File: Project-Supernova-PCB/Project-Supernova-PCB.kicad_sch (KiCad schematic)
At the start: 32 parts, among them J1 Conn_01x04, J103 Screw_Terminal_01x02, J104 Conn_01x02, J105 Conn_01x02, J106 Screw_Terminal_01x02, J107 Conn_Coaxial, J108 Conn_01x04, J109 Screw_Terminal_01x02, J6 100k_Thermistor, J7 100k_Thermistor, Q101 Si1470DH, SW1 SW_SPDT, U1 S09, U101 BMP280-Module, U102 GY-NEO6MV2-Module, U103 LoRa-E5, U2 ESP32-Module-30Pin, U3 LM335D

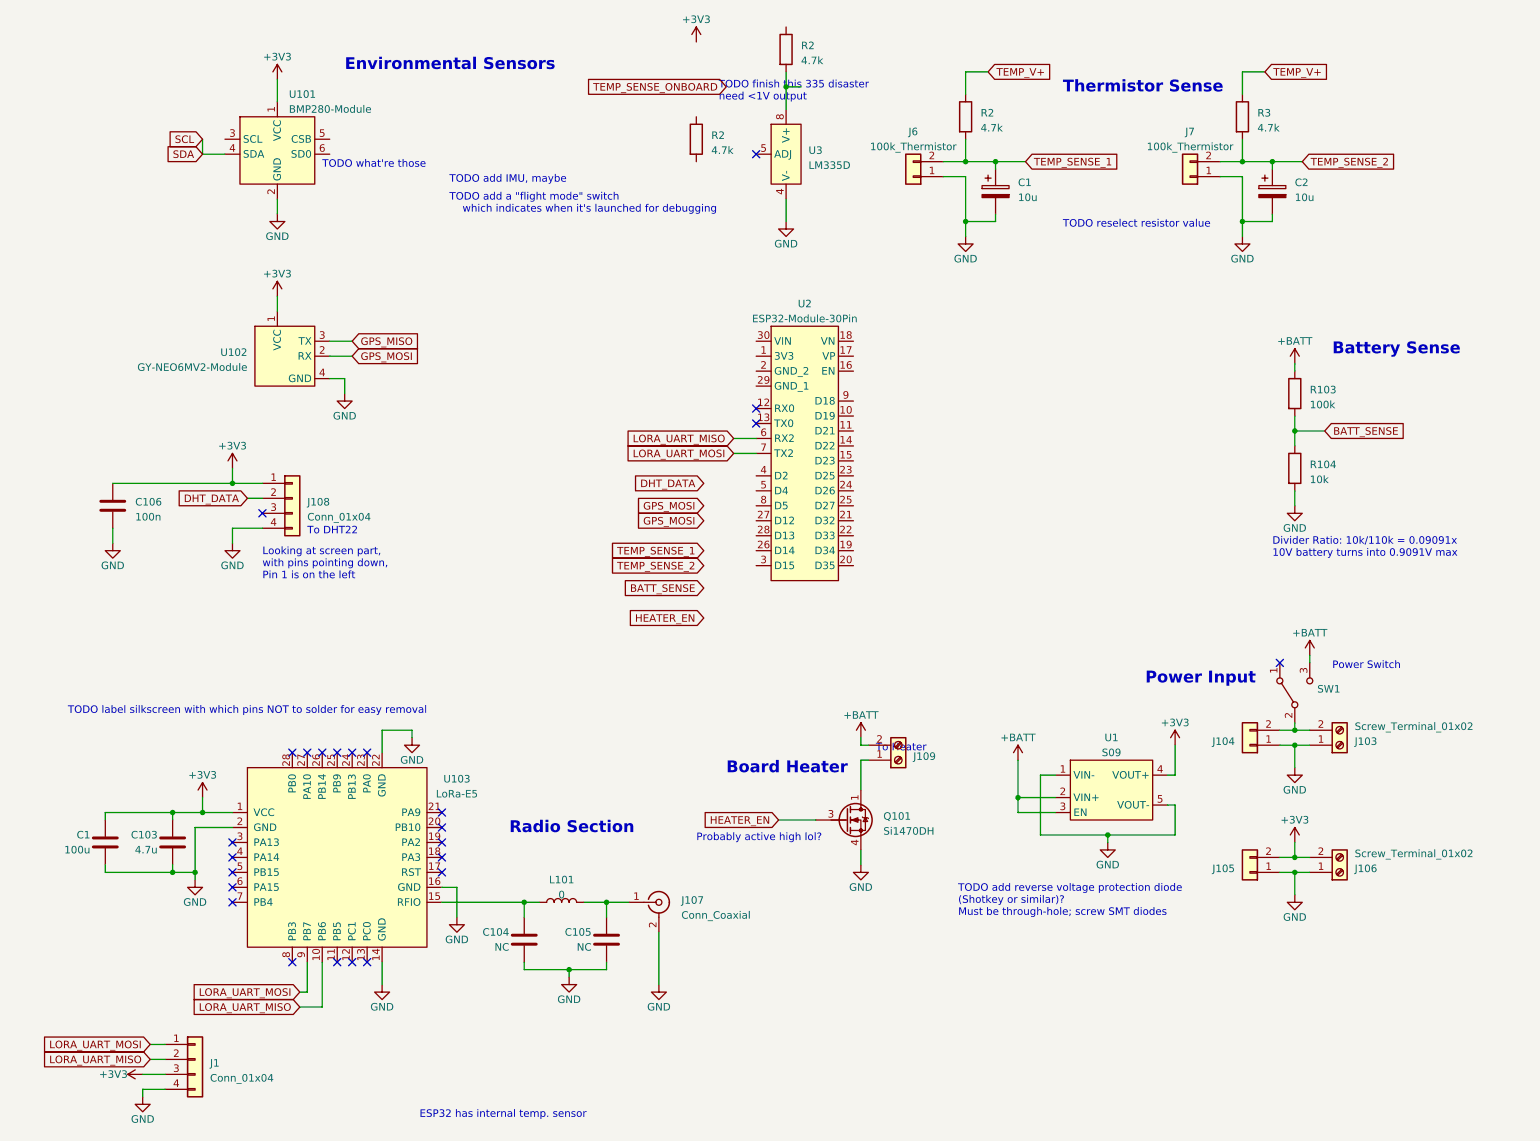
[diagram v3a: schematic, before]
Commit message: Add better LoRa footprint and better ESP symbol
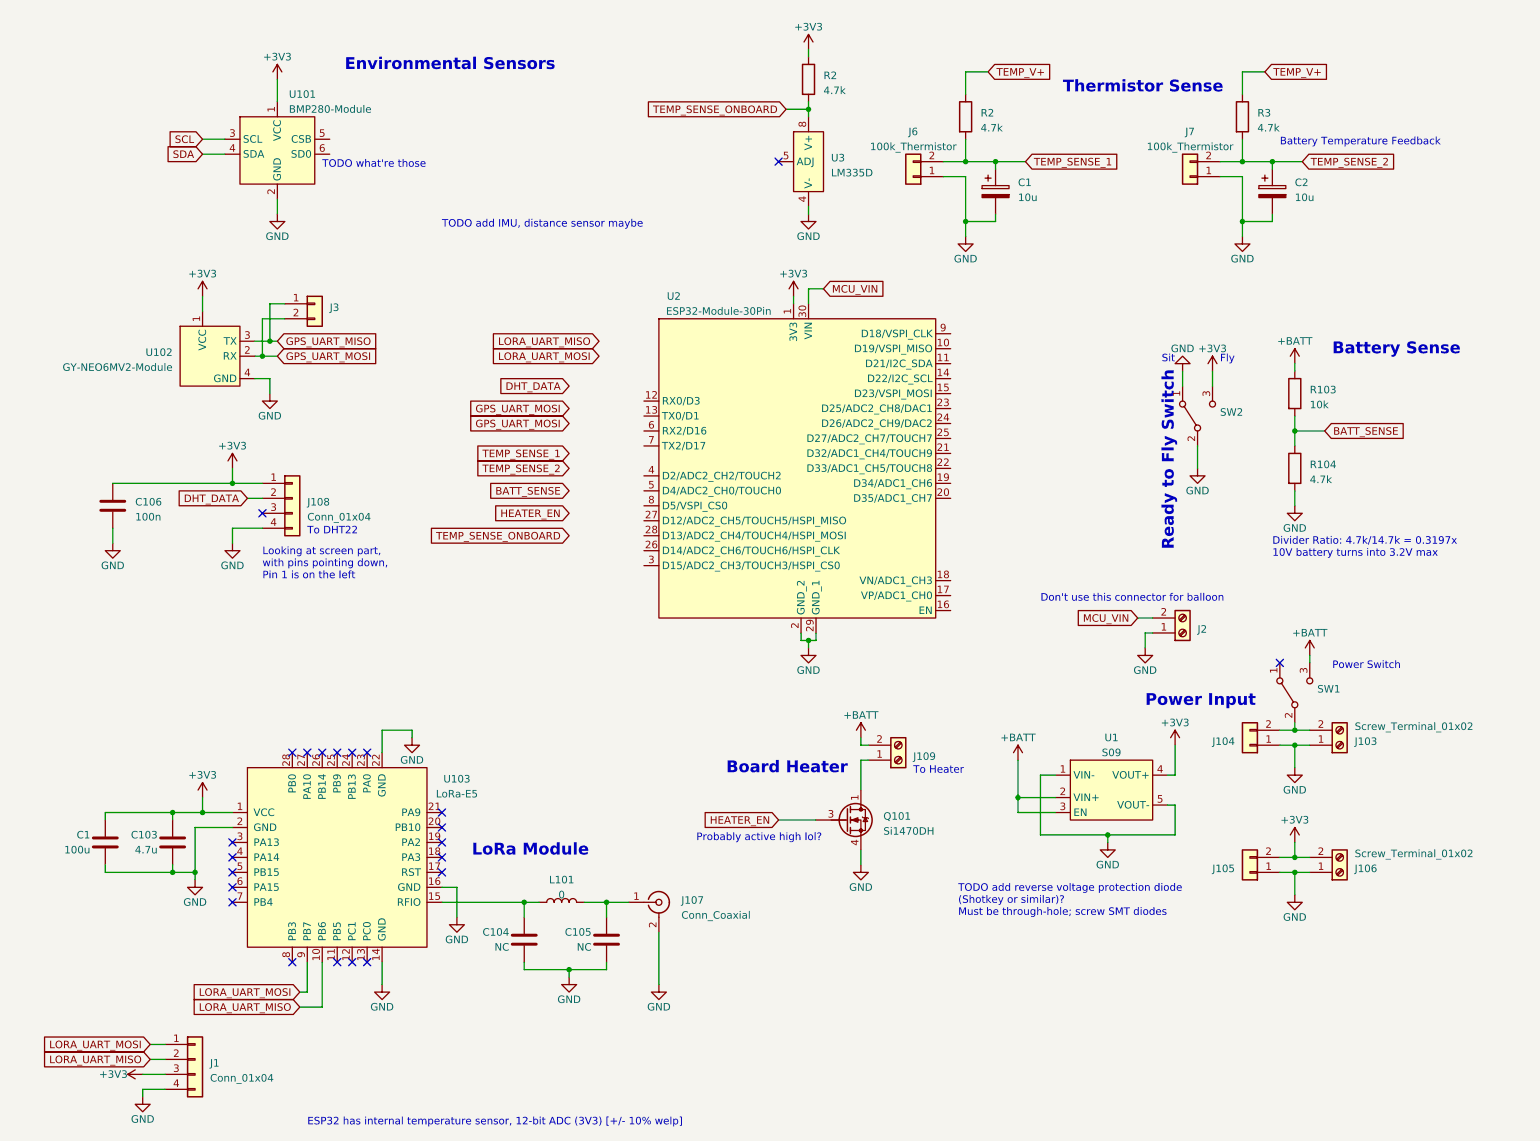
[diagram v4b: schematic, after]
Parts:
- removed R2: 4.7k, Resistor_SMD:R_1206_3216Metric_Pad1.30x1.75mm_HandSolder, symbol Device:R
- added J2: Screw_Terminal_01x02, TerminalBlock:TerminalBlock_bornier-2_P5.08mm, symbol Connector:Screw_Terminal_01x02
- added J3: Conn_01x02, symbol Connector_Generic:Conn_01x02
- added SW2: SW_SPDT, Button_Switch_THT:SW_Slide_1P2T_CK_OS102011MS2Q, symbol Switch:SW_SPDT
- R103: value 100k -> 10k
- R104: value 10k -> 4.7k
- U103: footprint Project-Supernova-Footprint-Lib:LoRa-E5 -> Project-Supernova-Footprint-Lib:LoRa-E5_HandSolder
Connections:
- net +3V3: now also R2.1, U2.1 (3V3), SW2.3 (C)
- net GND: now also U2.2 (GND_2), U2.29 (GND_1), J2.1 (Pin_1), SW2.1 (A), SW2.2 (B)
- net LORA_UART_MISO: no longer U2.6 (RX2)
- net LORA_UART_MOSI: no longer U2.7 (TX2)
- net SCL: now also U101.3 (SCL); no longer U101.4 (SDA)
- net TEMP_SENSE_ONBOARD: now also R2.2, U3.8 (V+)
- net MCU_VIN: now reaches U2.30 (VIN)
- net MCU_VIN: now also J2.2 (Pin_2)
- net GPS_MISO renamed GPS_UART_MISO
- net GPS_UART_MISO: now also J3.1 (Pin_1)
- net GPS_MOSI renamed GPS_UART_MOSI
- net GPS_UART_MOSI: now also J3.2 (Pin_2)
- new net SDA: U101.4 (SDA)
- no-connect marks 25 -> 23
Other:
- note added: "Battery Temperature Feedback"
- note added: "Divider Ratio: 4.7k/14.7k = 0.3197x 10V battery turns into 3.2V max"
- note added: "Don't use this connector for balloon"
- note added: "ESP32 has internal temperature sensor, 12-bit ADC (3V3) [+/- 10% welp]"
- note added: "Fly"
- note added: "LoRa Module"
- note added: "Ready to Fly Switch"
- note added: "Sit"
- note added: "TODO add IMU, distance sensor maybe"
- note removed: "Divider Ratio: 10k/110k = 0.09091x 10V battery turns into 0.9091V max"
- note removed: "ESP32 has internal temp. sensor"
- note removed: "Radio Section"
- note removed: "TODO add IMU, maybe"
- note removed: "TODO add a "flight mode" switch which indicates when it's launched for debugging"
- note removed: "TODO finish this 335 disaster need <1V output"
- note removed: "TODO label silkscreen with which pins NOT to solder for easy removal"
- note removed: "TODO reselect resistor value"
- moved on the sheet: R2, U102, U2, U3

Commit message: More work
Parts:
- removed J109: Screw_Terminal_01x02, TerminalBlock:TerminalBlock_bornier-2_P5.08mm, symbol Connector:Screw_Terminal_01x02
- removed Q101: Si1470DH, Package_TO_SOT_SMD:SOT-363_SC-70-6, symbol Transistor_FET:Si1442DH
- added J4: Screw_Terminal_01x02, TerminalBlock:TerminalBlock_bornier-2_P5.08mm, symbol Connector:Screw_Terminal_01x02
- added Q1: AO3420, Package_TO_SOT_SMD:SOT-23, symbol PCM_Transistor_MOSFET_AKL:AO3420
- J3: footprint (none) -> Connector_PinHeader_2.54mm:PinHeader_1x02_P2.54mm_Vertical
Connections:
- net +BATT: now also J4.2 (Pin_2)
- net GND: now also Q1.2 (S)
- net HEATER_EN: now also Q1.1 (G)
- new net: J4.1 (Pin_1), Q1.3 (D)
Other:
- note removed: "TODO add reverse voltage protection diode (Shotkey or similar)? Must be through-hole; screw SMT diodes"

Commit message: Connected MCU pins
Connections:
- net BATT_SENSE: now also U2.25 (D27/ADC2_CH7/TOUCH7)
- net DHT_DATA: now also U2.27 (D12/ADC2_CH5/TOUCH5/HSPI_MISO)
- net GND: no longer SW2.2 (B)
- net GPS_UART_MOSI: now also U2.4 (D2/ADC2_CH2/TOUCH2), U2.5 (D4/ADC2_CH0/TOUCH0)
- net HEATER_EN: now also U2.26 (D14/ADC2_CH6/TOUCH6/HSPI_CLK)
- net LORA_UART_MISO: now also U2.6 (RX2/D16)
- net LORA_UART_MOSI: now also U2.7 (TX2/D17)
- net SCL: now also U2.14 (D22/I2C_SCL)
- net SDA: now also U2.11 (D21/I2C_SDA)
- net TEMP_SENSE_1: now also U2.22 (D33/ADC1_CH5/TOUCH8)
- net TEMP_SENSE_2: now also U2.21 (D32/ADC1_CH4/TOUCH9)
- net TEMP_SENSE_ONBOARD: now also U2.19 (D34/ADC1_CH6)
- net TEMP_V+: now also U2.20 (D35/ADC1_CH7)
- net RTF_SWITCH: now reaches U2.9 (D18/VSPI_CLK)
- net RTF_SWITCH: now also SW2.2 (B)
- no-connect marks 23 -> 37
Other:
- note removed: "TODO what're those"

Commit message: Lay out PCB
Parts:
- added H1, H2, H3, H4: MountingHole_Pad, MountingHole:MountingHole_3.2mm_M3_DIN965_Pad, symbol Mechanical:MountingHole_Pad
- renumbered C106 to C2, C103 to C3, C104 to C4, C105 to C5, J105 to J10, J103 to J11, J106 to J12, J108 to J2, J107 to J4, J4 to J6, J2 to J7, J104 to J9, L101 to L1, R103 to R4, R104 to R5, SW2 to SW1, SW1 to SW2, U102 to U1, U101 to U2, U103 to U3, U3 to U4, U2 to U5, U1 to U6
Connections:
- net GND: now also H1.1, H2.1, H3.1, H4.1
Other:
- note removed: "TODO add IMU, distance sensor maybe"

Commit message: Routed PCB
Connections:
- net GPS_UART_MISO: now also U5.5 (D4/ADC2_CH0/TOUCH0)
- net GPS_UART_MOSI: no longer U5.5 (D4/ADC2_CH0/TOUCH0)
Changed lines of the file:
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@@
-    )
-  )
-  (global_label "GPS_UART_MOSI" (shape input) (at 113.03 95.25 180) (fields_autoplaced)
-    (effects (font (size 1.27 1.27)) (justify right))
-    (property "Intersheetrefs" "${INTERSHEET_REFS}" (at 95.1866 95.25 0)
-      (effects (font (size 1.27 1.27)) (justify right) hide)
     )
   )
@@
       (effects (font (size 1.27 1.27)) (justify right) hide)
     )
+  )
+  (global_label "GPS_UART_MISO" (shape input) (at 113.03 95.25 180) (fields_autoplaced)
+    (effects (font (size 1.27 1.27)) (justify right))
+    (property "Intersheetrefs" "${INTERSHEET_REFS}" (at 95.1866 95.25 0)
+      (effects (font (size 1.27 1.27)) (justify right) hide)
+    )
